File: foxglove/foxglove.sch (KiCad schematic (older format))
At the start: 17 parts, among them J1 NEIGHBOR1, J2 NEIGHBOR2, J3 RJ45, J7 BONUS_ROW, P1 CONN_02X05, U1 SHIFTER1, U2 SHIFTER2, U3 SHIFTER3, U4 SHIFTER4, U5 SHIFTER5, U6 SHIFTER6, U7 SHIFTER7, U8 SHIFTER8

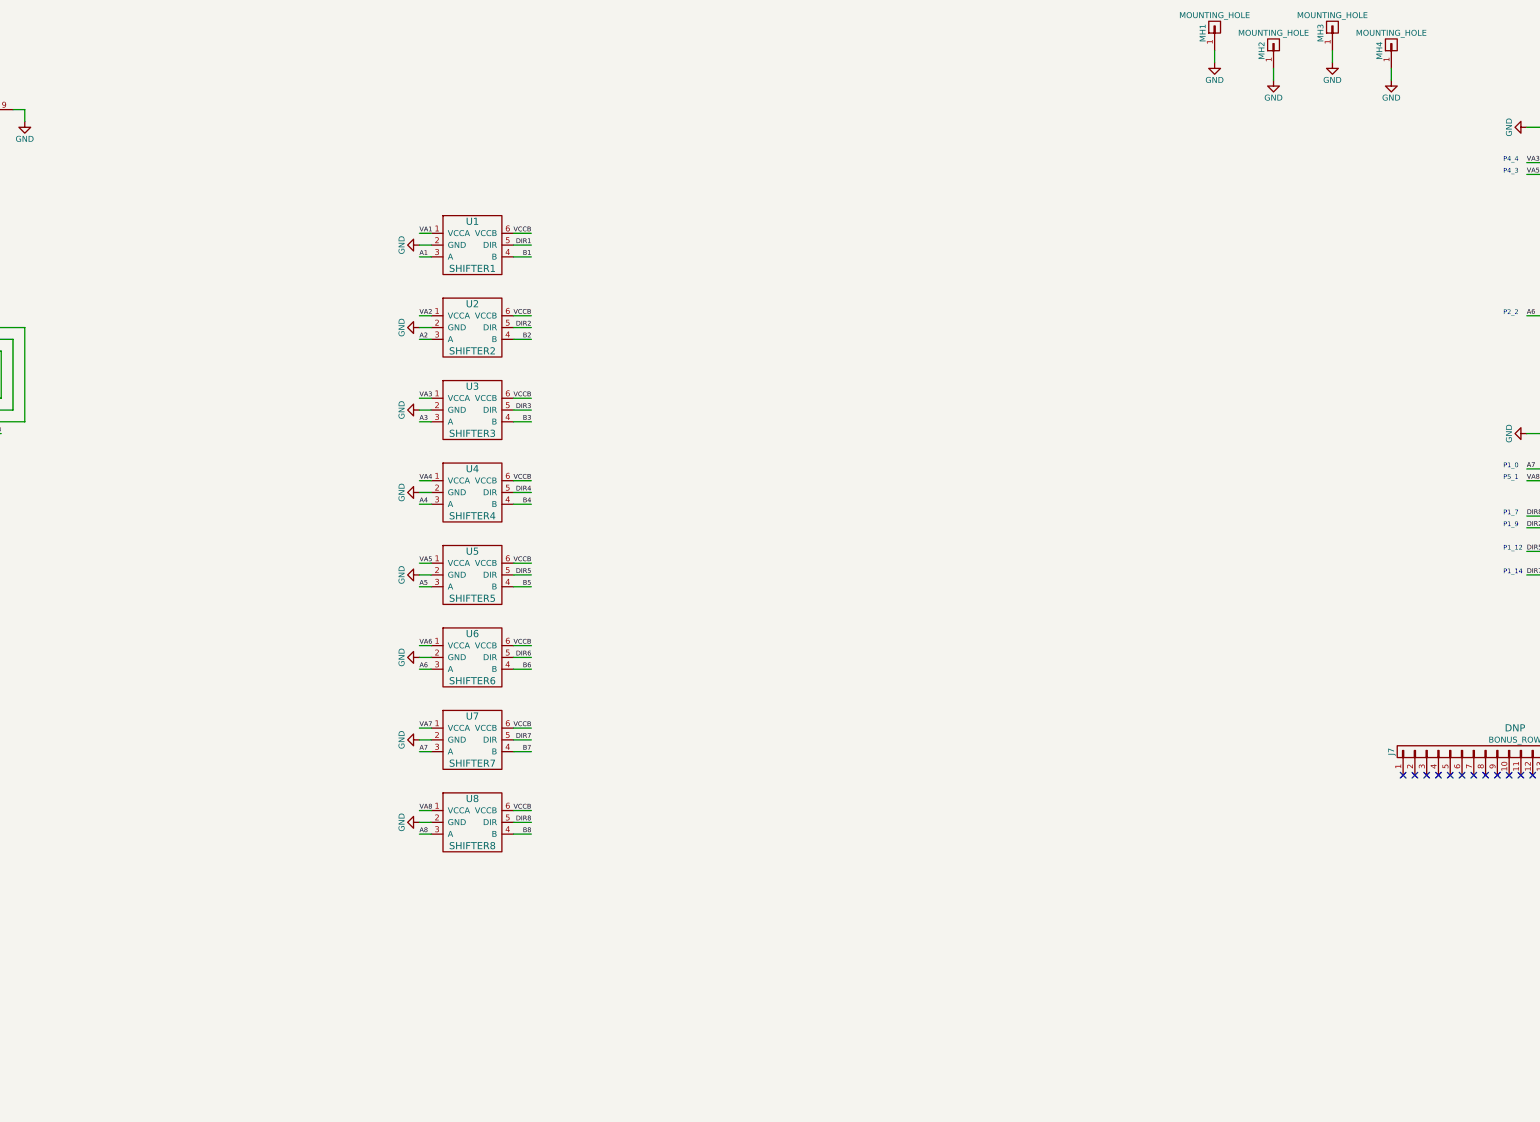
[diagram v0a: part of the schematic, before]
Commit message: Added greenPAK and iCE40 to schematic, started routing power connections
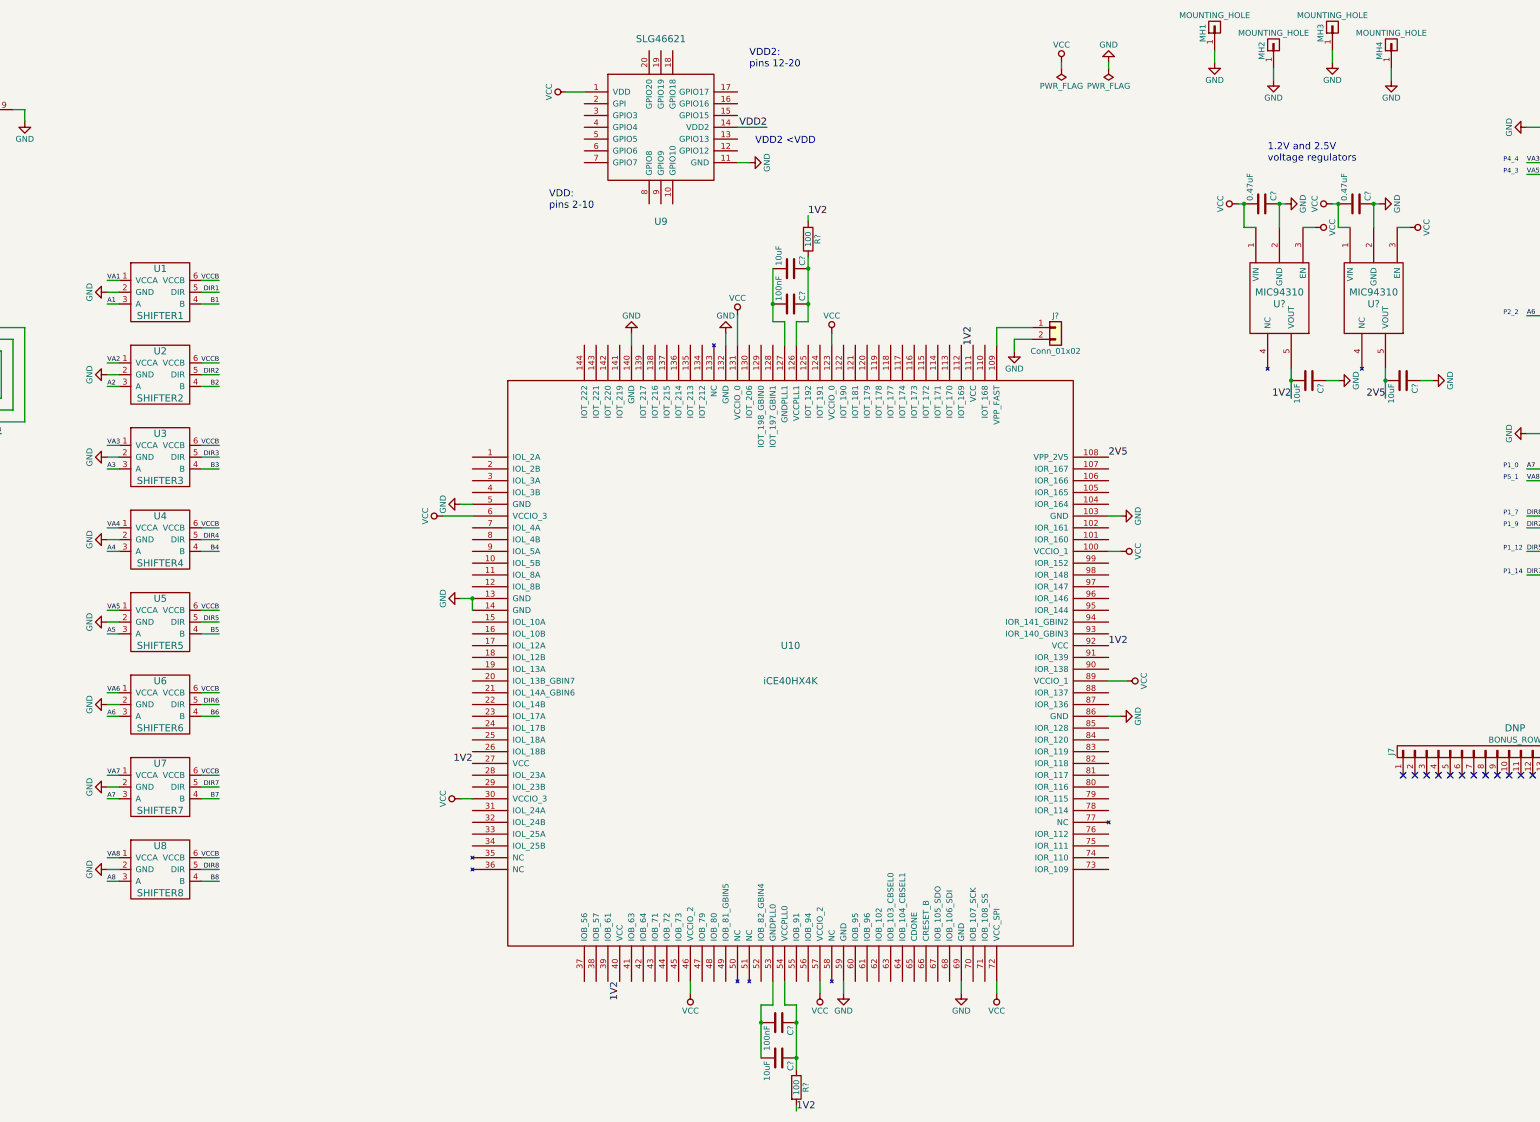
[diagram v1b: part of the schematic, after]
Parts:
- added C? (x4): 10uF, symbol C
- added C? (x2): 0.47uF, symbol C
- added C? (x2): 100nF, symbol C
- added J?: Conn_01x02, symbol Conn_01x02
- added R? (x2): 100, symbol R
- added U10: iCE40HX4K, gsg-modules:LQFP144, symbol iCE40HX4K
- added U9: SLG46621, gsg-modules:SLG46621, symbol SLG46621
- added U? (x2): MIC94310, symbol MIC94310
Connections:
- net GND: now also C?.1, C?.1, C?.1, C?.1, J?.2 (Pin_2), U10.103 (GND), U10.13 (GND), U10.132 (GND), U10.14 (GND), U10.140 (GND), U10.5 (GND), U10.59 (GND), U10.69 (GND), U10.86 (GND), U9.11 (GND), U?.2 (GND), U?.2 (GND)
- net VCC: now also C?.2, C?.2, U10.100 (VCCIO_1), U10.123 (VCCIO_0), U10.131 (VCCIO_0), U10.30 (VCCIO_3), U10.46 (VCCIO_2), U10.57 (VCCIO_2), U10.6 (VCCIO_3), U10.72 (VCC_SPI), U10.89 (VCCIO_1), U9.1 (VDD), U?.1 (VIN), U?.1 (VIN), U?.3 (EN), U?.3 (EN)
- new net: J?.1 (Pin_1), U10.109 (VPP_FAST)
- new net: C?.1, C?.1, R?.1, U10.126 (VCCPLL1)
- new net: C?.2, C?.2, U10.127 (GNDPLL1)
- new net: C?.2, C?.2, U10.53 (GNDPLL0)
- new net: C?.1, C?.1, R?.1, U10.54 (VCCPLL0)
- new net 1V2: C?.2, R?.2, R?.2, U10.111 (VCC), U10.27 (VCC), U10.40 (VCC), U10.92 (VCC), U?.5 (VOUT)
- new net 2V5: C?.2, U10.108 (VPP_2V5), U?.5 (VOUT)
- new net VDD2: U9.14 (VDD2)
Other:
- note added: "1.2V and 2.5V\nvoltage regulators"
- note added: "VDD2 <VDD"
- note added: "VDD2: \npins 12-20"
- note added: "VDD: \npins 2-10"
- moved on the sheet: U1, U2, U3, U4, U5, U6, U7, U8
